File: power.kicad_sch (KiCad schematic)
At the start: 43 parts, among them J1 KYCON_KPJX-4S-S, J2 MicroFit_2x02, J3 24V/5A OUT, J3B1 DNI, Q1 BC847, Q2 IRF9540SPBF, Q3 BC857, SW1 DNI, U1 MC78M12CDT-TR, U2 MAX5035BUSA

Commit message: LED city
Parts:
- R10: value (none) -> 130K
- R12: value (none) -> 220K
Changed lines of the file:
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@@
     (in_bom yes) (on_board yes)
     (property "Reference" "R10" (id 0) (at 162.56 91.44 90))
-    (property "Value" "" (id 1) (at 162.56 88.9 90))
+    (property "Value" "130K" (id 1) (at 162.56 88.9 90))
     (property "Footprint" "Resistor_SMD:R_0603_1608Metric" (id 2) (at 162.56 90.678 90)
       (effects (font (size 1.27 1.27)) hide)
@@
     (in_bom yes) (on_board yes)
     (property "Reference" "R12" (id 0) (at 196.215 100.33 0))
-    (property "Value" "" (id 1) (at 193.04 101.6 90))
+    (property "Value" "220K" (id 1) (at 193.04 101.6 90))
     (property "Footprint" "Resistor_SMD:R_0603_1608Metric" (id 2) (at 191.262 101.6 90)
       (effects (font (size 1.27 1.27)) hide)

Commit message: Mostly groundplane declutter and loop removal.
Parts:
- added C10: 22u, Capacitor_SMD:C_1206_3216Metric, symbol Device:C
- renumbered C10 to C11
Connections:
- net GND: now also C10.1
- net U2_FB: now also C10.2
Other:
- moved on the sheet: C11
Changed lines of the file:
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@@
   (junction (at 157.48 68.58) (diameter 0) (color 0 0 0 0)
   )
-  (junction (at 256.54 101.6) (diameter 0) (color 0 0 0 0)
+  (junction (at 257.81 101.6) (diameter 0) (color 0 0 0 0)
   )
   (junction (at 48.26 27.94) (diameter 1.75) (color 194 0 0 1)
@@
   (junction (at 44.45 38.1) (diameter 0) (color 0 0 0 0)
   )
+  (junction (at 260.35 101.6) (diameter 0) (color 0 0 0 0)
+  )
   (junction (at 73.66 82.55) (diameter 0) (color 0 0 0 0)
   )
@@
     (stroke (width 0) (type default) (color 0 0 0 0))
   )
-  (wire (pts (xy 256.54 102.87) (xy 256.54 101.6))
+  (wire (pts (xy 257.81 102.87) (xy 257.81 101.6))
     (stroke (width 0) (type default) (color 0 0 0 0))
   )
@@
     (stroke (width 0) (type default) (color 0 0 0 0))
   )
-  (wire (pts (xy 250.19 101.6) (xy 256.54 101.6))
+  (wire (pts (xy 250.19 101.6) (xy 257.81 101.6))
     (stroke (width 0) (type default) (color 0 0 0 0))
   )
@@
     (stroke (width 0.8) (type solid) (color 0 0 0 0))
   )
+  (wire (pts (xy 261.62 101.6) (xy 260.35 101.6))
+    (stroke (width 0) (type default) (color 0 0 0 0))
+  )
   (wire (pts (xy 27.94 186.69) (xy 25.4 186.69))
     (stroke (width 0) (type default) (color 0 0 0 0))
@@
     (stroke (width 0) (type default) (color 0 0 0 0))
   )
-  (wire (pts (xy 256.54 110.49) (xy 256.54 111.76))
+  (wire (pts (xy 257.81 110.49) (xy 257.81 111.76))
     (stroke (width 0) (type default) (color 0 0 0 0))
   )
-  (wire (pts (xy 256.54 101.6) (xy 260.35 101.6))
+  (wire (pts (xy 257.81 101.6) (xy 260.35 101.6))
     (stroke (width 0) (type default) (color 0 0 0 0))
   )
@@
     (stroke (width 0) (type default) (color 0 0 0 0))
   )
+  (wire (pts (xy 250.19 111.125) (xy 250.19 112.395))
+    (stroke (width 0) (type default) (color 0 0 0 0))
+  )
   (wire (pts (xy 158.75 29.21) (xy 158.75 26.67))
     (stroke (width 0) (type default) (color 0 0 0 0))
@@
     (stroke (width 0) (type default) (color 0 0 0 0))
   )
+  (wire (pts (xy 250.19 101.6) (xy 250.19 103.505))
+    (stroke (width 0) (type default) (color 0 0 0 0))
+  )
   (polyline (pts (xy 82.55 142.24) (xy 83.82 139.7))
     (stroke (width 0.8) (type solid) (color 0 0 0 0))
@@
     (pin "2")
   )
-  (symbol (lib_id "power:GND") (at 256.54 111.76 0) (unit 1)
+  (symbol (lib_id "power:GND") (at 257.81 111.76 0) (unit 1)
     (in_bom yes) (on_board yes)
-    (property "Reference" "#PWR012" (id 0) (at 256.54 118.11 0)
+    (property "Reference" "#PWR013" (id 0) (at 257.81 118.11 0)
       (effects (font (size 1.27 1.27)) hide)
     )
-    (property "Value" "GND" (id 1) (at 256.54 115.57 0))
-    (property "Footprint" "" (id 2) (at 256.54 111.76 0)
+    (property "Value" "GND" (id 1) (at 257.81 115.57 0))
+    (property "Footprint" "" (id 2) (at 257.81 111.76 0)
       (effects (font (size 1.27 1.27)) hide)
     )
-    (property "Datasheet" "" (id 3) (at 256.54 111.76 0)
+    (property "Datasheet" "" (id 3) (at 257.81 111.76 0)
       (effects (font (size 1.27 1.27)) hide)
     )
@@
     (pin "1")
   )
+  (symbol (lib_id "Device:C") (at 250.19 107.315 180) (unit 1)
+    (in_bom yes) (on_board yes)
+    (property "Reference" "C10" (id 0) (at 252.095 105.41 0))
+    (property "Value" "22u" (id 1) (at 252.095 109.855 0))
+    (property "Footprint" "Capacitor_SMD:C_1206_3216Metric" (id 2) (at 249.2248 103.505 0)
+      (effects (font (size 1.27 1.27)) hide)
+    )
+    (property "Datasheet" "" (id 3) (at 250.19 107.315 0)
+      (effects (font (size 1.27 1.27)) hide)
+    )
+    (property "E14MOQ" "10" (id 5) (at 250.19 107.315 0)
+      (effects (font (size 1.27 1.27)) hide)
+    )
+    (property "JLCMFR#" "CC0603KRX7R9BB104" (id 7) (at 250.19 107.315 0)
+      (effects (font (size 1.27 1.27)) hide)
+    )
+    (property "JLCMOQ" "20" (id 8) (at 250.19 107.315 0)
+      (effects (font (size 1.27 1.27)) hide)
+    )
+    (property "JLCPART" "C14663" (id 9) (at 250.19 107.315 0)
+      (effects (font (size 1.27 1.27)) hide)
+    )
+    (pin "1")
+    (pin "2")
+  )
   (symbol (lib_id "Device:R") (at 73.66 88.9 0) (unit 1)
     (in_bom yes) (on_board yes)
@@
   (symbol (lib_id "power:+5V") (at 271.78 98.425 0) (unit 1)
     (in_bom yes) (on_board yes)
-    (property "Reference" "#PWR013" (id 0) (at 271.78 102.235 0)
+    (property "Reference" "#PWR014" (id 0) (at 271.78 102.235 0)
       (effects (font (size 1.27 1.27)) hide)
     )
@@
     (pin "2")
   )
-  (symbol (lib_id "Device:C_Polarized_US") (at 256.54 106.68 0) (unit 1)
+  (symbol (lib_id "Device:C_Polarized_US") (at 257.81 106.68 0) (unit 1)
     (in_bom yes) (on_board yes)
-    (property "Reference" "C10" (id 0) (at 259.08 105.41 0)
+    (property "Reference" "C11" (id 0) (at 258.445 104.775 0)
       (effects (font (size 1.27 1.27)) (justify left))
     )
-    (property "Value" "68u/35V" (id 1) (at 259.08 107.95 0)
+    (property "Value" "68u/35V" (id 1) (at 258.445 109.855 0)
       (effects (font (size 1.27 1.27)) (justify left))
     )
-    (property "Footprint" "-Project:CP_Elec_6.3x7.7_DOT" (id 2) (at 256.54 106.68 0)
+    (property "Footprint" "-Project:CP_Elec_6.3x7.7_DOT" (id 2) (at 257.81 106.68 0)
       (effects (font (size 1.27 1.27)) hide)
     )
-    (property "Datasheet" "https://www.farnell.com/datasheets/2606991.pdf" (id 3) (at 256.54 106.68 0)
+    (property "Datasheet" "https://www.farnell.com/datasheets/2606991.pdf" (id 3) (at 257.81 106.68 0)
       (effects (font (size 1.27 1.27)) hide)
     )
-    (property "E14MOQ" "1" (id 5) (at 256.54 106.68 0)
+    (property "E14MOQ" "1" (id 5) (at 257.81 106.68 0)
       (effects (font (size 1.27 1.27)) hide)
     )
-    (property "LCSC" "" (id 6) (at 256.54 106.68 0)
+    (property "LCSC" "" (id 6) (at 257.81 106.68 0)
       (effects (font (size 1.27 1.27)) hide)
     )
-    (property "LCSCMFR#" "" (id 7) (at 256.54 106.68 0)
+    (property "LCSCMFR#" "" (id 7) (at 257.81 106.68 0)
       (effects (font (size 1.27 1.27)) hide)
     )
-    (property "JLCPART" "C178649" (id 8) (at 256.54 106.68 0)
+    (property "JLCPART" "C178649" (id 8) (at 257.81 106.68 0)
       (effects (font (size 1.27 1.27)) hide)
     )
-    (property "JLCMFR#" "EEHZC1V680XP" (id 9) (at 256.54 106.68 0)
+    (property "JLCMFR#" "EEHZC1V680XP" (id 9) (at 257.81 106.68 0)
       (effects (font (size 1.27 1.27)) hide)
     )
-    (property "JLCMOQ" "2" (id 10) (at 256.54 106.68 0)
+    (property "JLCMOQ" "2" (id 10) (at 257.81 106.68 0)
       (effects (font (size 1.27 1.27)) hide)
     )
@@
     (pin "3")
   )
+  (symbol (lib_id "power:GND") (at 250.19 112.395 0) (unit 1)
+    (in_bom yes) (on_board yes)
+    (property "Reference" "#PWR012" (id 0) (at 250.19 118.745 0)
+      (effects (font (size 1.27 1.27)) hide)
+    )
+    (property "Value" "GND" (id 1) (at 250.19 116.205 0))
+    (property "Footprint" "" (id 2) (at 250.19 112.395 0)
+      (effects (font (size 1.27 1.27)) hide)
+    )
+    (property "Datasheet" "" (id 3) (at 250.19 112.395 0)
+      (effects (font (size 1.27 1.27)) hide)
+    )
+    (pin "1")
+  )
   (symbol (lib_id "3rd-party:NT_2_TT") (at 262.89 101.6 0) (unit 1)

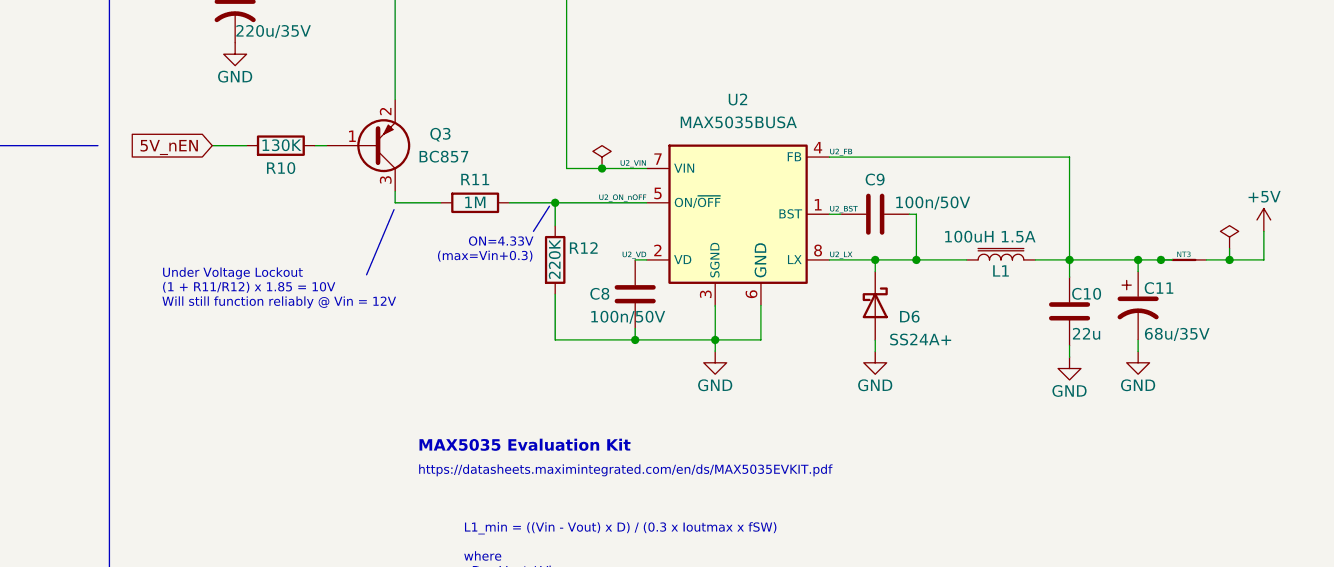
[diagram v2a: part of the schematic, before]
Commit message: More ground plane clearance/optimization.
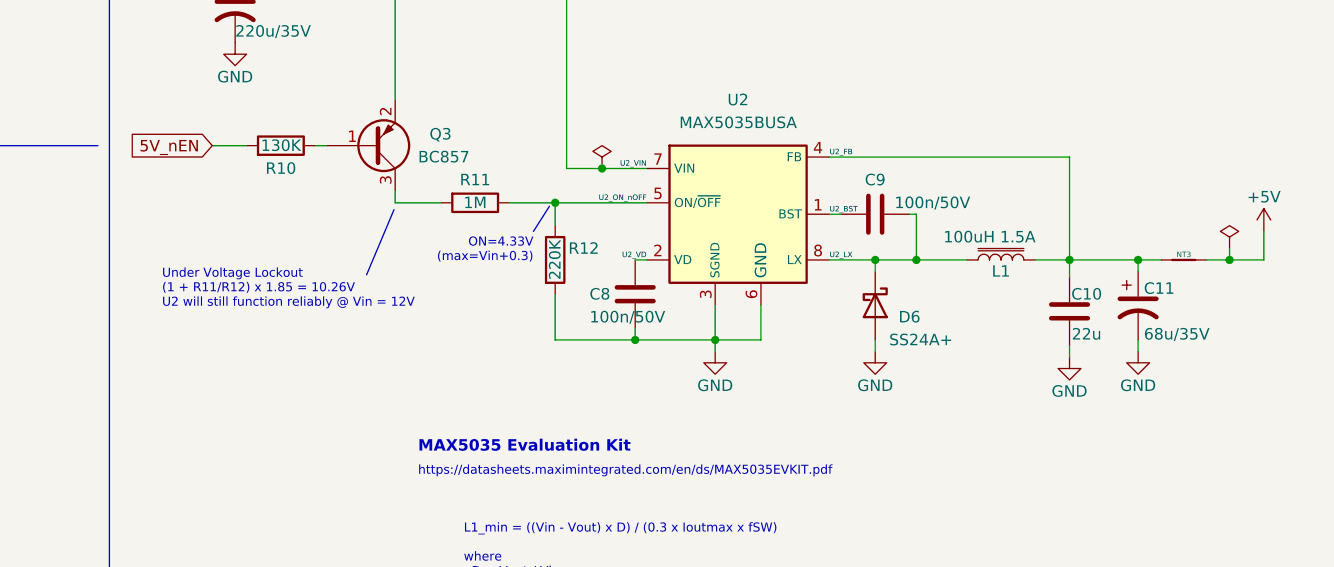
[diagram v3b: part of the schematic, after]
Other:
- note added: "Under Voltage Lockout (1 + R11/R12) x 1.85 = 10.26V U2 will still function reliably @ Vin = 12V"
- note removed: "Under Voltage Lockout (1 + R11/R12) x 1.85 = 10V Will still function reliably @ Vin = 12V"
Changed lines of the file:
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@@
   (junction (at 44.45 38.1) (diameter 0) (color 0 0 0 0)
   )
-  (junction (at 260.35 101.6) (diameter 0) (color 0 0 0 0)
-  )
   (junction (at 73.66 82.55) (diameter 0) (color 0 0 0 0)
   )
@@
     (stroke (width 0.8) (type solid) (color 0 0 0 0))
   )
-  (wire (pts (xy 261.62 101.6) (xy 260.35 101.6))
-    (stroke (width 0) (type default) (color 0 0 0 0))
-  )
   (wire (pts (xy 27.94 186.69) (xy 25.4 186.69))
     (stroke (width 0) (type default) (color 0 0 0 0))
@@
     )
   )
-  (text "Under Voltage Lockout\n(1 + R11/R12) x 1.85 = 10V\nWill still function reliably @ Vin = 12V\n"
+  (text "Under Voltage Lockout\n(1 + R11/R12) x 1.85 = 10.26V\nU2 will still function reliably @ Vin = 12V\n"
     (at 149.352 107.061 0)
     (effects (font (size 1 1)) (justify left bottom))

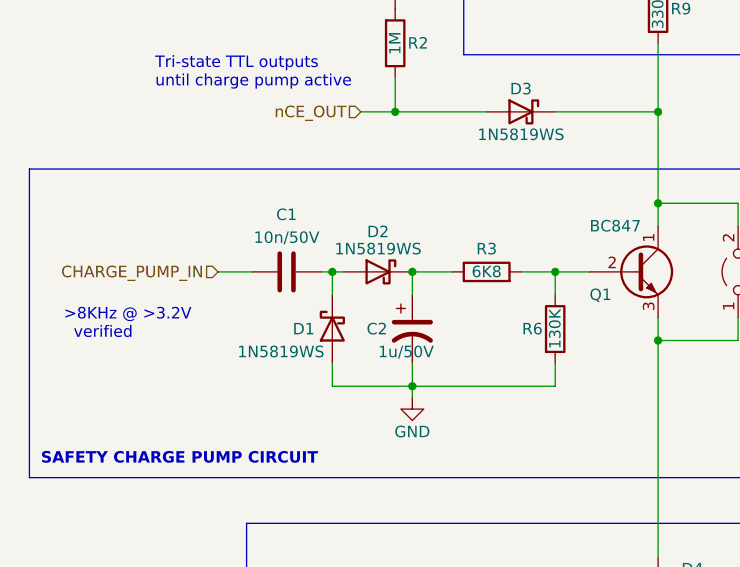
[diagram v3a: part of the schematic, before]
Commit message: Moving charge pump 15KHz input closer to source,
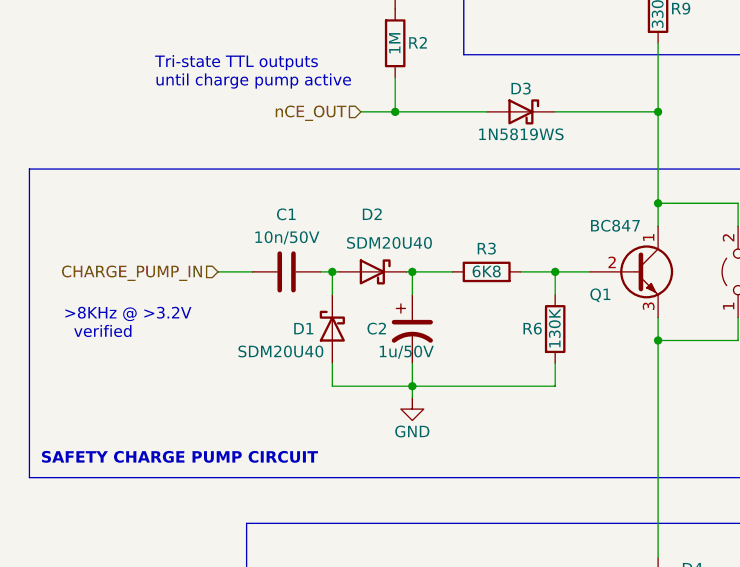
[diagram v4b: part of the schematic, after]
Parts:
- D1, D2: value 1N5819WS -> SDM20U40; footprint -Project:D_SOD-323_DOT -> Diode_SMD:D_SOD-523; JLCMFR# 1N5819WS -> SDM20U40-7; JLCMOQ 5 -> 15; JLCPART C191023 -> C139439
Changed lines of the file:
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@@
     (stroke (width 0) (type default) (color 0 0 0 0))
   )
+  (wire (pts (xy 57.15 82.55) (xy 57.785 82.55))
+    (stroke (width 0) (type default) (color 0 0 0 0))
+  )
   (wire (pts (xy 85.09 27.94) (xy 85.09 29.21))
     (stroke (width 0) (type default) (color 0 0 0 0))
@@
     (stroke (width 1) (type default) (color 194 0 0 1))
   )
-  (wire (pts (xy 48.895 82.55) (xy 50.165 82.55))
+  (wire (pts (xy 48.895 82.55) (xy 49.53 82.55))
     (stroke (width 0) (type default) (color 0 0 0 0))
   )
@@
     (pin "1")
   )
+  (symbol (lib_id "Device:D_Schottky") (at 53.34 82.55 0) (mirror y) (unit 1)
+    (in_bom yes) (on_board yes)
+    (property "Reference" "D2" (id 0) (at 53.34 76.2 0))
+    (property "Value" "SDM20U40" (id 1) (at 55.245 79.375 0))
+    (property "Footprint" "Diode_SMD:D_SOD-523" (id 2) (at 53.34 82.55 0)
+      (effects (font (size 1.27 1.27)) hide)
+    )
+    (property "Datasheet" "https://datasheet.lcsc.com/lcsc/1809192039_Diodes-Incorporated-SDM20U40-7_C139439.pdf" (id 3) (at 53.34 82.55 0)
+      (effects (font (size 1.27 1.27)) hide)
+    )
+    (property "JLCPART" "C139439" (id 4) (at 53.34 82.55 0)
+      (effects (font (size 1.27 1.27)) hide)
+    )
+    (property "JLCMFR#" "SDM20U40-7" (id 5) (at 53.34 82.55 0)
+      (effects (font (size 1.27 1.27)) hide)
+    )
+    (property "JLCMOQ" "15" (id 6) (at 53.34 82.55 0)
+      (effects (font (size 1.27 1.27)) hide)
+    )
+    (pin "1")
+    (pin "2")
+  )
   (symbol (lib_id "Connector:Conn_01x02_Female") (at 114.3 27.94 0) (unit 1)
     (in_bom yes) (on_board yes)
@@
     (in_bom yes) (on_board yes)
     (property "Reference" "D1" (id 0) (at 45.72 88.9 90))
-    (property "Value" "1N5819WS" (id 1) (at 43.18 91.44 90))
-    (property "Footprint" "-Project:D_SOD-323_DOT" (id 2) (at 48.895 88.9 0)
+    (property "Value" "SDM20U40" (id 1) (at 43.18 91.44 90))
+    (property "Footprint" "Diode_SMD:D_SOD-523" (id 2) (at 48.895 88.9 0)
       (effects (font (size 1.27 1.27)) hide)
     )
-    (property "Datasheet" "https://datasheet.lcsc.com/lcsc/1810202112_Guangdong-Hottech-1N5819WS_C191023.pdf" (id 3) (at 48.895 88.9 0)
+    (property "Datasheet" "https://datasheet.lcsc.com/lcsc/1809192039_Diodes-Incorporated-SDM20U40-7_C139439.pdf" (id 3) (at 48.895 88.9 0)
       (effects (font (size 1.27 1.27)) hide)
     )
-    (property "JLCPART" "C191023" (id 4) (at 48.895 88.9 0)
+    (property "JLCPART" "C139439" (id 4) (at 48.895 88.9 0)
       (effects (font (size 1.27 1.27)) hide)
     )
-    (property "JLCMFR#" "1N5819WS" (id 5) (at 48.895 88.9 0)
+    (property "JLCMFR#" "SDM20U40-7" (id 5) (at 48.895 88.9 0)
       (effects (font (size 1.27 1.27)) hide)
     )
-    (property "JLCMOQ" "5" (id 6) (at 48.895 88.9 0)
+    (property "JLCMOQ" "15" (id 6) (at 48.895 88.9 0)
       (effects (font (size 1.27 1.27)) hide)
     )
@@
     (pin "1")
   )
-  (symbol (lib_id "Device:D_Schottky") (at 53.975 82.55 0) (mirror y) (unit 1)
-    (in_bom yes) (on_board yes)
-    (property "Reference" "D2" (id 0) (at 53.975 78.105 0))
-    (property "Value" "1N5819WS" (id 1) (at 53.975 80.01 0))
-    (property "Footprint" "-Project:D_SOD-323_DOT" (id 2) (at 53.975 82.55 0)
-      (effects (font (size 1.27 1.27)) hide)
-    )
-    (property "Datasheet" "https://datasheet.lcsc.com/lcsc/1810202112_Guangdong-Hottech-1N5819WS_C191023.pdf" (id 3) (at 53.975 82.55 0)
-      (effects (font (size 1.27 1.27)) hide)
-    )
-    (property "JLCPART" "C191023" (id 4) (at 53.975 82.55 0)
-      (effects (font (size 1.27 1.27)) hide)
-    )
-    (property "Note" "" (id 10) (at 53.975 82.55 0)
-      (effects (font (size 1.27 1.27)) hide)
-    )
-    (property "JLCMFR#" "1N5819WS" (id 11) (at 53.975 82.55 0)
-      (effects (font (size 1.27 1.27)) hide)
-    )
-    (property "JLCMOQ" "5" (id 12) (at 53.975 82.55 0)
-      (effects (font (size 1.27 1.27)) hide)
-    )
-    (pin "1")
-    (pin "2")
-  )
   (symbol (lib_id "power:PWR_FLAG") (at 48.26 22.86 0) (mirror y) (unit 1)
